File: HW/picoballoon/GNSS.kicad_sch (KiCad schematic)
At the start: 7 parts, among them Q1 NDT452AP, U3 MAX-M8C

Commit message: aprs test board
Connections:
- net TX: now reaches U3.2 (TXD)
- net RX: now reaches U3.3 (RXD)
- net GNSS_EN renamed EN
- net GNSS_EXTINT renamed EXTINT
- net GNSS_RESET renamed RESET
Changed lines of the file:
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@@
+	(wire
+		(pts
+			(xy 119.38 96.52) (xy 124.46 96.52)
+		)
+		(stroke
+			(width 0)
+			(type default)
+		)
+	)
+	(wire
+		(pts
+			(xy 127 69.85) (xy 127 72.39)
+		)
+		(stroke
+			(width 0)
+			(type default)
+		)
+	)
+	(wire
+		(pts
+			(xy 137.16 58.42) (xy 137.16 59.69)
+		)
+		(stroke
+			(width 0)
+			(type default)
+		)
+	)
+	(wire
+		(pts
+			(xy 144.78 162.56) (xy 144.78 161.29)
+		)
+		(stroke
+			(width 0)
+			(type default)
+		)
+	)
+	(wire
+		(pts
+			(xy 133.35 161.29) (xy 144.78 161.29)
+		)
+		(stroke
+			(width 0)
+			(type default)
+		)
+	)
+	(wire
+		(pts
+			(xy 133.35 170.18) (xy 133.35 172.72)
+		)
+		(stroke
+			(width 0)
+			(type default)
+		)
+	)
 	(wire
 		(pts
@@
 	(wire
 		(pts
-			(xy 127 69.85) (xy 127 72.39)
-		)
-		(stroke
-			(width 0)
-			(type default)
-		)
-	)
-	(wire
-		(pts
-			(xy 137.16 58.42) (xy 137.16 59.69)
-		)
-		(stroke
-			(width 0)
-			(type default)
-		)
-	)
-	(wire
-		(pts
-			(xy 144.78 162.56) (xy 144.78 161.29)
-		)
-		(stroke
-			(width 0)
-			(type default)
-		)
-	)
-	(wire
-		(pts
-			(xy 133.35 161.29) (xy 144.78 161.29)
-		)
-		(stroke
-			(width 0)
-			(type default)
-		)
-	)
-	(wire
-		(pts
-			(xy 133.35 170.18) (xy 133.35 172.72)
-		)
-		(stroke
-			(width 0)
-			(type default)
-		)
-	)
-	(wire
-		(pts
 			(xy 127 59.69) (xy 137.16 59.69)
 		)
@@
 			(width 0)
 			(type default)
+		)
+	)
+	(wire
+		(pts
+			(xy 119.38 93.98) (xy 124.46 93.98)
+		)
+		(stroke
+			(width 0)
+			(type default)
+		)
+	)
+	(hierarchical_label "EN"
+		(shape input)
+		(at 113.03 72.39 180)
+		(fields_autoplaced yes)
+		(effects
+			(font
+				(size 1.27 1.27)
+			)
+			(justify right)
+		)
+	)
+	(hierarchical_label "RESET"
+		(shape input)
+		(at 119.38 114.3 180)
+		(fields_autoplaced yes)
+		(effects
+			(font
+				(size 1.27 1.27)
+			)
+			(justify right)
+		)
+	)
+	(hierarchical_label "EXTINT"
+		(shape input)
+		(at 119.38 109.22 180)
+		(fields_autoplaced yes)
+		(effects
+			(font
+				(size 1.27 1.27)
+			)
+			(justify right)
+		)
+	)
+	(hierarchical_label "SCL"
+		(shape input)
+		(at 119.38 104.14 180)
+		(fields_autoplaced yes)
+		(effects
+			(font
+				(size 1.27 1.27)
+			)
+			(justify right)
+		)
+	)
+	(hierarchical_label "RX"
+		(shape input)
+		(at 119.38 93.98 180)
+		(fields_autoplaced yes)
+		(effects
+			(font
+				(size 1.27 1.27)
+			)
+			(justify right)
 		)
 	)
@@
 		)
 	)
-	(hierarchical_label "GNSS_EN"
-		(shape input)
-		(at 113.03 72.39 180)
-		(fields_autoplaced yes)
-		(effects
-			(font
-				(size 1.27 1.27)
-			)
-			(justify right)
-		)
-	)
-	(hierarchical_label "GNSS_RESET"
-		(shape input)
-		(at 119.38 114.3 180)
-		(fields_autoplaced yes)
-		(effects
-			(font
-				(size 1.27 1.27)
-			)
-			(justify right)
-		)
-	)
-	(hierarchical_label "GNSS_EXTINT"
-		(shape input)
-		(at 119.38 109.22 180)
-		(fields_autoplaced yes)
-		(effects
-			(font
-				(size 1.27 1.27)
-			)
-			(justify right)
-		)
-	)
-	(hierarchical_label "SCL"
-		(shape input)
-		(at 119.38 104.14 180)
-		(fields_autoplaced yes)
-		(effects
+	(hierarchical_label "TX"
+		(shape output)
+		(at 119.38 96.52 180)
+		(fields_autoplaced yes)
+		(effects

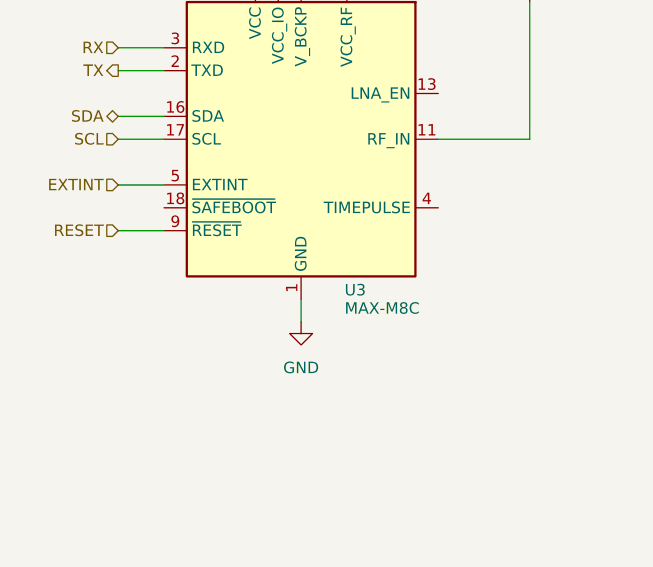
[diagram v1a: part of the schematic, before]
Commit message: some devices replaced
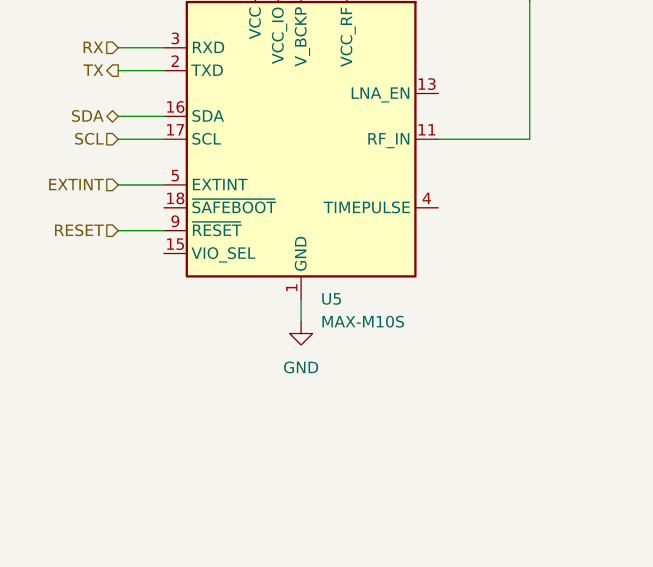
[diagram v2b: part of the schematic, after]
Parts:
- removed U3: MAX-M8C, RF_GPS:ublox_MAX, symbol RF_GPS:MAX-M8C
- added U5: MAX-M10S, RF_GPS:ublox_MAX, symbol RF_GPS:MAX-M10S
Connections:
- net EXTINT: now also U5.5 (EXTINT)
- net GND: now also U5.1 (GND), U5.10 (GND), U5.12 (GND)
- net RESET: now also U5.9 (~{RESET})
- net RX: now also U5.3 (RXD)
- net SCL: now also U5.17 (SCL)
- net SDA: now also U5.16 (SDA)
- net TX: now also U5.2 (TXD)
- net at AE1.1 (A): now also U5.11 (RF_IN)
- net at Q1.1 (D): now also U5.6 (V_BCKP), U5.7 (VCC_IO), U5.8 (VCC)
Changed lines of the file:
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@@
+	)
+	(symbol
+		(lib_id "RF_GPS:MAX-M10S")
+		(at 139.7 104.14 0)
+		(unit 1)
+		(exclude_from_sim no)
+		(in_bom yes)
+		(on_board yes)
+		(dnp no)
+		(fields_autoplaced yes)
+		(property "Reference" "U5"
+			(at 141.8941 121.92 0)
+			(effects
+				(font
+					(size 1.27 1.27)
+				)
+				(justify left)
+			)
+		)
+		(property "Value" "MAX-M10S"
+			(at 141.8941 124.46 0)
+			(effects
+				(font
+					(size 1.27 1.27)
+				)
+				(justify left)
+			)
+		)
+		(property "Footprint" "RF_GPS:ublox_MAX"
+			(at 149.86 120.65 0)
+			(effects
+				(font
+					(size 1.27 1.27)
+				)
+				(hide yes)
+			)
+		)
+		(property "Datasheet" "https://content.u-blox.com/sites/default/files/MAX-M10S_DataSheet_UBX-20035208.pdf"
+			(at 139.7 104.14 0)
+			(effects
+				(font
+					(size 1.27 1.27)
+				)
+				(hide yes)
+			)
+		)
+		(property "Description" "GNSS Module MAX M10, VCC 1.65V to 3.6V"
+			(at 139.7 104.14 0)
+			(effects
+				(font
+					(size 1.27 1.27)
+				)
+				(hide yes)
+			)
+		)
+		(pin "13"
+		)
+		(pin "3"
+		)
+		(pin "15"
+		)
+		(pin "5"
+		)
+		(pin "6"
+		)
+		(pin "2"
+		)
+		(pin "10"
+		)
+		(pin "4"
+		)
+		(pin "8"
+		)
+		(pin "16"
+		)
+		(pin "17"
+		)
+		(pin "9"
+		)
+		(pin "14"
+		)
+		(pin "7"
+		)
+		(pin "11"
+		)
+		(pin "12"
+		)
+		(pin "18"
+		)
+		(pin "1"
+		)
+		(instances
+			(project ""
+				(path "/f2ac4b1c-d093-4228-80b2-7ee26b75b20f/5f4497d1-ad88-4b05-809e-a165ed29847c"
+					(reference "U5")
+					(unit 1)
+				)
+			)
+		)
 	)
 	(symbol
@@
 					(unit 1)
 				)
-			)
-		)
-	)
-	(symbol
-		(lib_id "RF_GPS:MAX-M8C")
-		(at 139.7 104.14 0)
-		(unit 1)
-		(exclude_from_sim no)
-		(in_bom yes)
-		(on_board yes)
-		(dnp no)
-		(property "Reference" "U3"
-			(at 144.526 120.904 0)
-			(effects
-				(font
-					(size 1.27 1.27)
-				)
-				(justify left)
-			)
-		)
-		(property "Value" "MAX-M8C"
-			(at 144.526 122.936 0)
-			(effects
-				(font
-					(size 1.27 1.27)
-				)
-				(justify left)
-			)
-		)
-		(property "Footprint" "RF_GPS:ublox_MAX"
-			(at 149.86 120.65 0)
-			(effects
-				(font
-					(size 1.27 1.27)
-				)
-				(hide yes)
-			)
-		)
-		(property "Datasheet" "https://www.u-blox.com/sites/default/files/MAX-M8-FW3_DataSheet_%28UBX-15031506%29.pdf"
-			(at 139.7 104.14 0)
-			(effects
-				(font
-					(size 1.27 1.27)
-				)
-				(hide yes)
-			)
-		)
-		(property "Description" "GNSS Module MAX M8, VCC 1.65V to 3.6V"
-			(at 139.7 104.14 0)
-			(effects
-				(font
-					(size 1.27 1.27)
-				)
-				(hide yes)
-			)
-		)
-		(pin "17"
-		)
-		(pin "15"
-		)
-		(pin "18"
-		)
-		(pin "12"
-		)
-		(pin "4"
-		)
-		(pin "16"
-		)
-		(pin "7"
-		)
-		(pin "10"
-		)
-		(pin "5"
-		)
-		(pin "1"
-		)
-		(pin "6"
-		)
-		(pin "14"
-		)
-		(pin "3"
-		)
-		(pin "13"
-		)
-		(pin "2"
-		)
-		(pin "8"
-		)
-		(pin "9"
-		)
-		(pin "11"
-		)
-		(instances
-			(project "picoballoon"
-				(path "/f2ac4b1c-d093-4228-80b2-7ee26b75b20f/5f4497d1-ad88-4b05-809e-a165ed29847c"
-					(reference "U3")
-					(unit 1)
-				)

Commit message: pcb
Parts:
- removed Q1: NDT452AP, symbol Simulation_SPICE:PMOS
- removed R2: 10k, symbol Device:R
- removed R6: 875, symbol Device:R
- C4, C5: footprint (none) -> Capacitor_SMD:C_0603_1608Metric_Pad1.08x0.95mm_HandSolder
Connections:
- net +3.3V: now also U5.6 (V_BCKP), U5.7 (VCC_IO), U5.8 (VCC)

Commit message: picoballoon pcb
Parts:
- AE1: footprint (none) -> Library:RECE20369001E01
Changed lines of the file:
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@@
 			)
 		)
-		(property "Footprint" ""
+		(property "Footprint" "Library:RECE20369001E01"
 			(at 165.1 83.82 0)
 			(effects

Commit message: test points
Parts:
- renumbered C4 to C24, C5 to C25
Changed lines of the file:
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@@
 		(on_board yes)
 		(dnp no)
-		(property "Reference" "C4"
+		(property "Reference" "C24"
 			(at 135.89 165.1 0)
 			(effects
@@
 			(project "picoballoon"
 				(path "/f2ac4b1c-d093-4228-80b2-7ee26b75b20f/5f4497d1-ad88-4b05-809e-a165ed29847c"
-					(reference "C4")
+					(reference "C24")
 					(unit 1)
 				)
@@
 		(on_board yes)
 		(dnp no)
-		(property "Reference" "C5"
+		(property "Reference" "C25"
 			(at 147.32 165.1 0)
 			(effects
@@
 			(project "picoballoon"
 				(path "/f2ac4b1c-d093-4228-80b2-7ee26b75b20f/5f4497d1-ad88-4b05-809e-a165ed29847c"
-					(reference "C5")
+					(reference "C25")
 					(unit 1)
 				)

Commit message: APRS testing with Arduinno
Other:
- company: (none) -> Vojtech Piroch
- title: (none) -> GNSS
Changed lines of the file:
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@@
 	(generator_version "8.0")
 	(paper "A4")
+	(title_block
+		(title "GNSS")
+		(date "2025-01-03")
+		(company "Vojtech Piroch")
+	)
 	(junction
 		(at 137.16 83.82)
